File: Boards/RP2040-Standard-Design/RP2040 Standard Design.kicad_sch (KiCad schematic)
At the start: 37 parts, among them J1 BM03B-SRSS-TBLFSN, J3 USB_C, SW1 SW_Push, SW3 SW_Push, U1 ESD7L5.0DT5G, U2 ST1L05APU33R

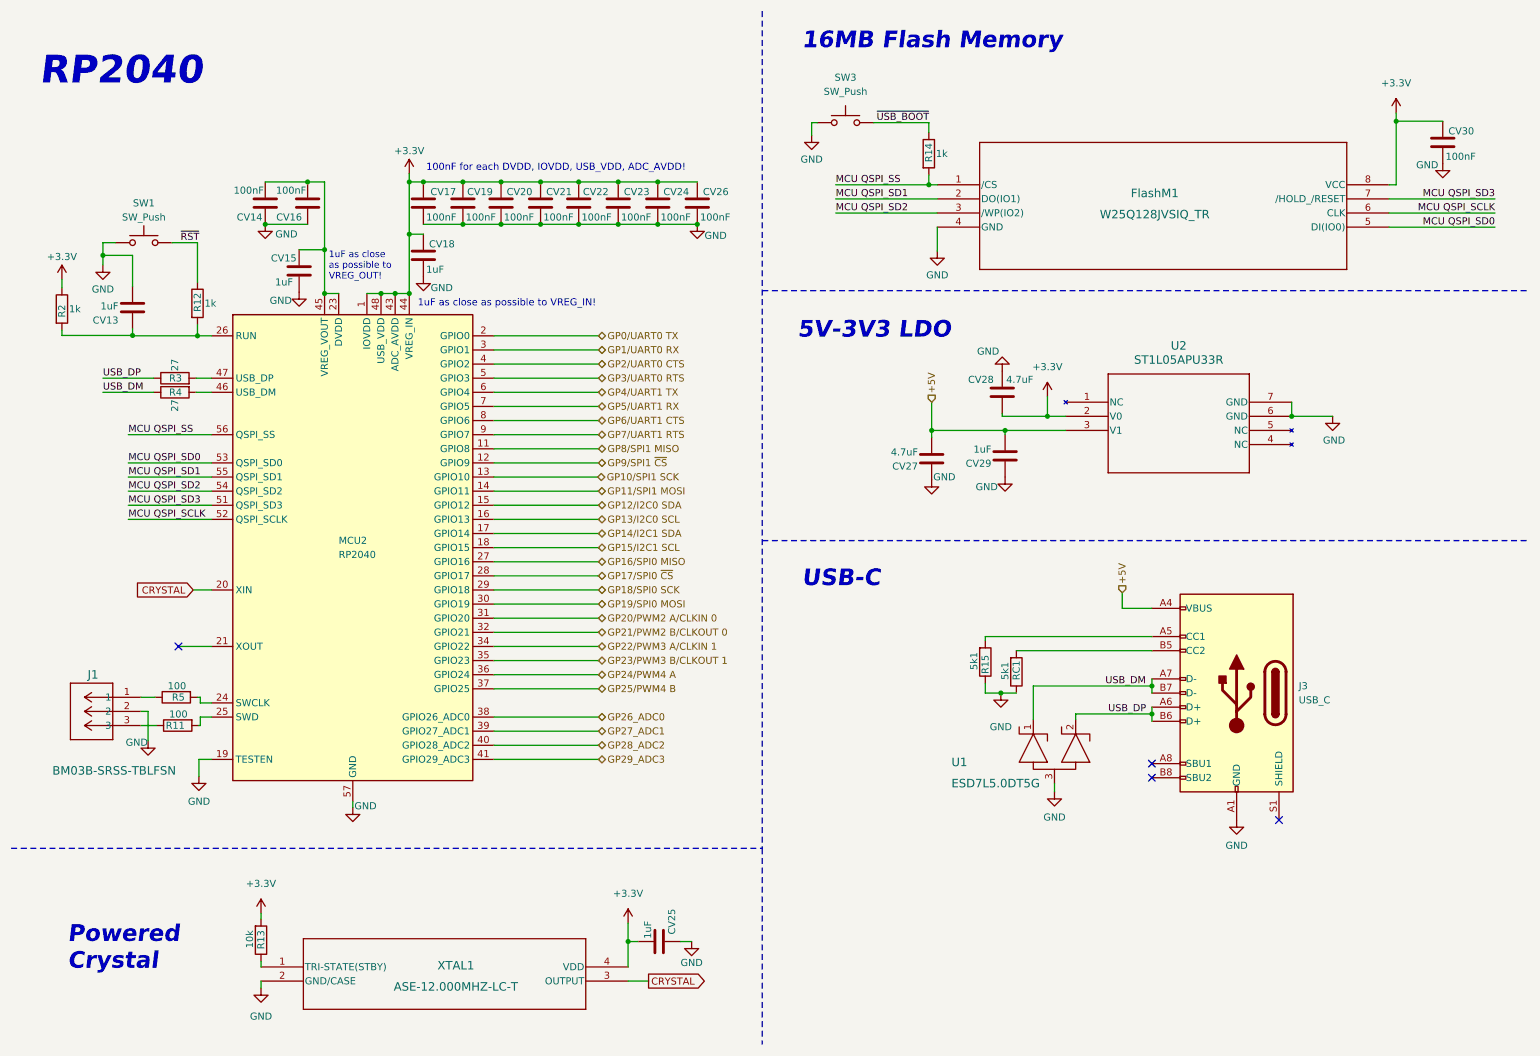
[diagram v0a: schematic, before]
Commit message: Preparação do RP2040 para PCB Design
Foram corrigidos todos os ERC errors e warnings. Foram feitas alterações
aos necessários simbolos, e foi adicionado um botão na biblioteca de
simbolos
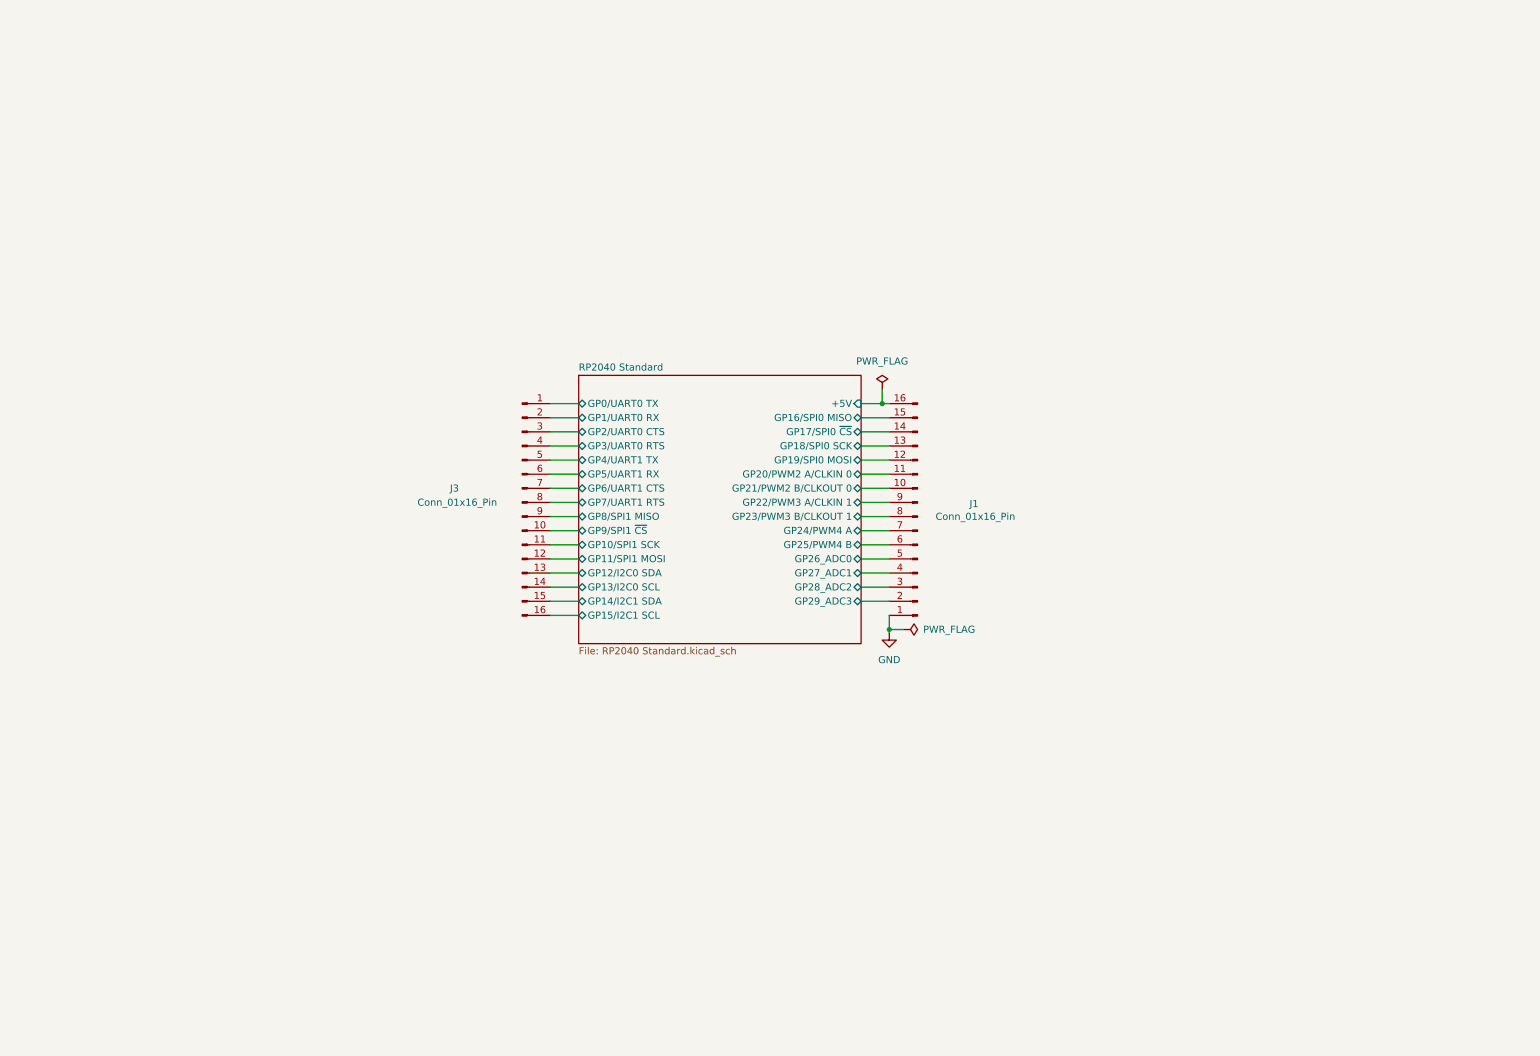
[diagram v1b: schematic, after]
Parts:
- removed CV13, CV15, CV18, CV25, CV29: 1uF, Capacitor_SMD:C_0201_0603Metric, symbol Device:C
- removed CV14, CV16, CV17, CV19, CV20, CV21, CV22, CV23, CV24, CV26, CV30: 100nF, Capacitor_SMD:C_0201_0603Metric, symbol Device:C
- removed CV27, CV28: 4.7uF, Capacitor_SMD:C_0201_0603Metric, symbol Device:C
- removed FlashM1: W25Q128JVSIQ_TR, SOIC_208MIL_WIN, symbol W25Q128JVSIQ TR:W25Q128JVSIQ_TR
- removed J1: BM03B-SRSS-TBLFSN, CONN_BM03B-SRSS-TBLFSN_JST, symbol SWD Con:BM03B-SRSS-TBLFSN
- removed J3: USB_C, Connector_USB:USB_C_Plug_JAE_DX07P024AJ1, symbol Connector:USB_C_Receptacle_USB2.0
- removed MCU2: RP2040, Package_DFN_QFN:QFN-56-1EP_7x7mm_P0.4mm_EP3.2x3.2mm, symbol MCU_RaspberryPi:RP2040
- removed R11, R5: 100, Resistor_SMD:R_0201_0603Metric, symbol Device:R
- removed R12, R14, R2: 1k, Resistor_SMD:R_0201_0603Metric, symbol Device:R
- removed R13: 10k, Resistor_SMD:R_0201_0603Metric, symbol Device:R
- removed R15, RC1: 5k1, Resistor_SMD:R_0201_0603Metric, symbol Device:R
- removed R3, R4: 27, Resistor_SMD:R_0201_0603Metric, symbol Device:R
- removed SW1, SW3: SW_Push, Button_Switch_SMD:SW_Push_1P1T-MP_NO_Horizontal_Alps_SKRTLAE010, symbol Switch:SW_Push
- removed U1: ESD7L5.0DT5G, SOT-723_0P85X1P25_ONS, symbol ESD Protection Diode:ESD7L5.0DT5G
- removed U2: ST1L05APU33R, DFN_5APU33R_STM, symbol LDO 5V.3V3:ST1L05APU33R
- removed XTAL1: ASE-12.000MHZ-LC-T, ASE-3.2X2.5_ABR, symbol AS12MHz:ASE-12.000MHZ-LC-T
- added J1, J3: Conn_01x16_Pin, symbol Connector:Conn_01x16_Pin
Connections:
- net GND: now also J1.1 (Pin_1)
- new net RP2040 Standard/+5V: J1.16 (Pin_16)
- new net RP2040 Standard/GP0/UART0 TX: J3.1 (Pin_1)
- new net RP2040 Standard/GP10/SPI1 SCK: J3.11 (Pin_11)
- new net RP2040 Standard/GP11/SPI1 MOSI: J3.12 (Pin_12)
- new net RP2040 Standard/GP12/I2C0 SDA: J3.13 (Pin_13)
- new net RP2040 Standard/GP13/I2C0 SCL: J3.14 (Pin_14)
- new net RP2040 Standard/GP14/I2C1 SDA: J3.15 (Pin_15)
- new net RP2040 Standard/GP15/I2C1 SCL: J3.16 (Pin_16)
- new net RP2040 Standard/GP16/SPI0 MISO: J1.15 (Pin_15)
- new net RP2040 Standard/GP17/SPI0 ~{CS}: J1.14 (Pin_14)
- new net RP2040 Standard/GP18/SPI0 SCK: J1.13 (Pin_13)
- new net RP2040 Standard/GP19/SPI0 MOSI: J1.12 (Pin_12)
- new net RP2040 Standard/GP1/UART0 RX: J3.2 (Pin_2)
- new net RP2040 Standard/GP20/PWM2 A/CLKIN 0: J1.11 (Pin_11)
- new net RP2040 Standard/GP21/PWM2 B/CLKOUT 0: J1.10 (Pin_10)
- new net RP2040 Standard/GP22/PWM3 A/CLKIN 1: J1.9 (Pin_9)
- new net RP2040 Standard/GP23/PWM3 B/CLKOUT 1: J1.8 (Pin_8)
- new net RP2040 Standard/GP24/PWM4 A: J1.7 (Pin_7)
- new net RP2040 Standard/GP25/PWM4 B: J1.6 (Pin_6)
- new net RP2040 Standard/GP26_ADC0: J1.5 (Pin_5)
- new net RP2040 Standard/GP27_ADC1: J1.4 (Pin_4)
- new net RP2040 Standard/GP28_ADC2: J1.3 (Pin_3)
- new net RP2040 Standard/GP29_ADC3: J1.2 (Pin_2)
- new net RP2040 Standard/GP2/UART0 CTS: J3.3 (Pin_3)
- new net RP2040 Standard/GP3/UART0 RTS: J3.4 (Pin_4)
- new net RP2040 Standard/GP4/UART1 TX: J3.5 (Pin_5)
- new net RP2040 Standard/GP5/UART1 RX: J3.6 (Pin_6)
- new net RP2040 Standard/GP6/UART1 CTS: J3.7 (Pin_7)
- new net RP2040 Standard/GP7/UART1 RTS: J3.8 (Pin_8)
- new net RP2040 Standard/GP8/SPI1 MISO: J3.9 (Pin_9)
- new net RP2040 Standard/GP9/SPI1 ~{CS}: J3.10 (Pin_10)
- no-connect marks 4 -> 0
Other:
- added sheet RP2040 Standard (RP2040 Standard.kicad_sch)
- note removed: "100nF for each DVDD, IOVDD, USB_VDD, ADC_AVDD!"
- note removed: "16MB Flash Memory"
- note removed: "1uF as close as possible to VREG_IN!"
- note removed: "1uF as close as possible to VREG_OUT!"
- note removed: "5V-3V3 LDO"
- note removed: "Powered Crystal"
- note removed: "RP2040"
- note removed: "USB-C"

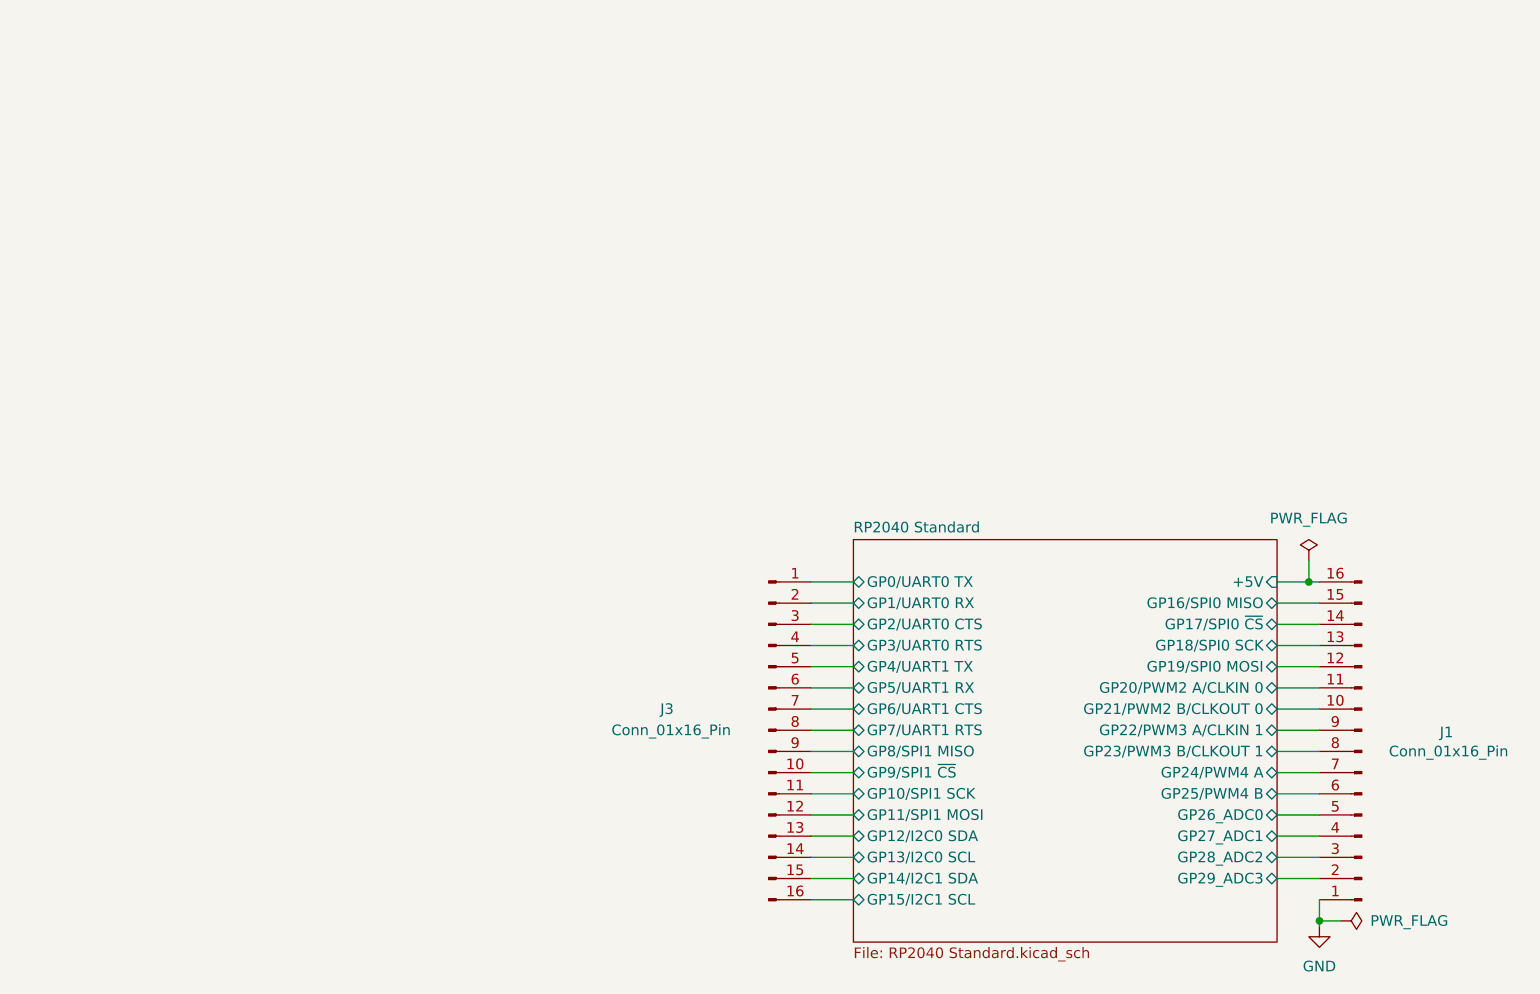
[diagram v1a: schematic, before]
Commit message: USB-C update
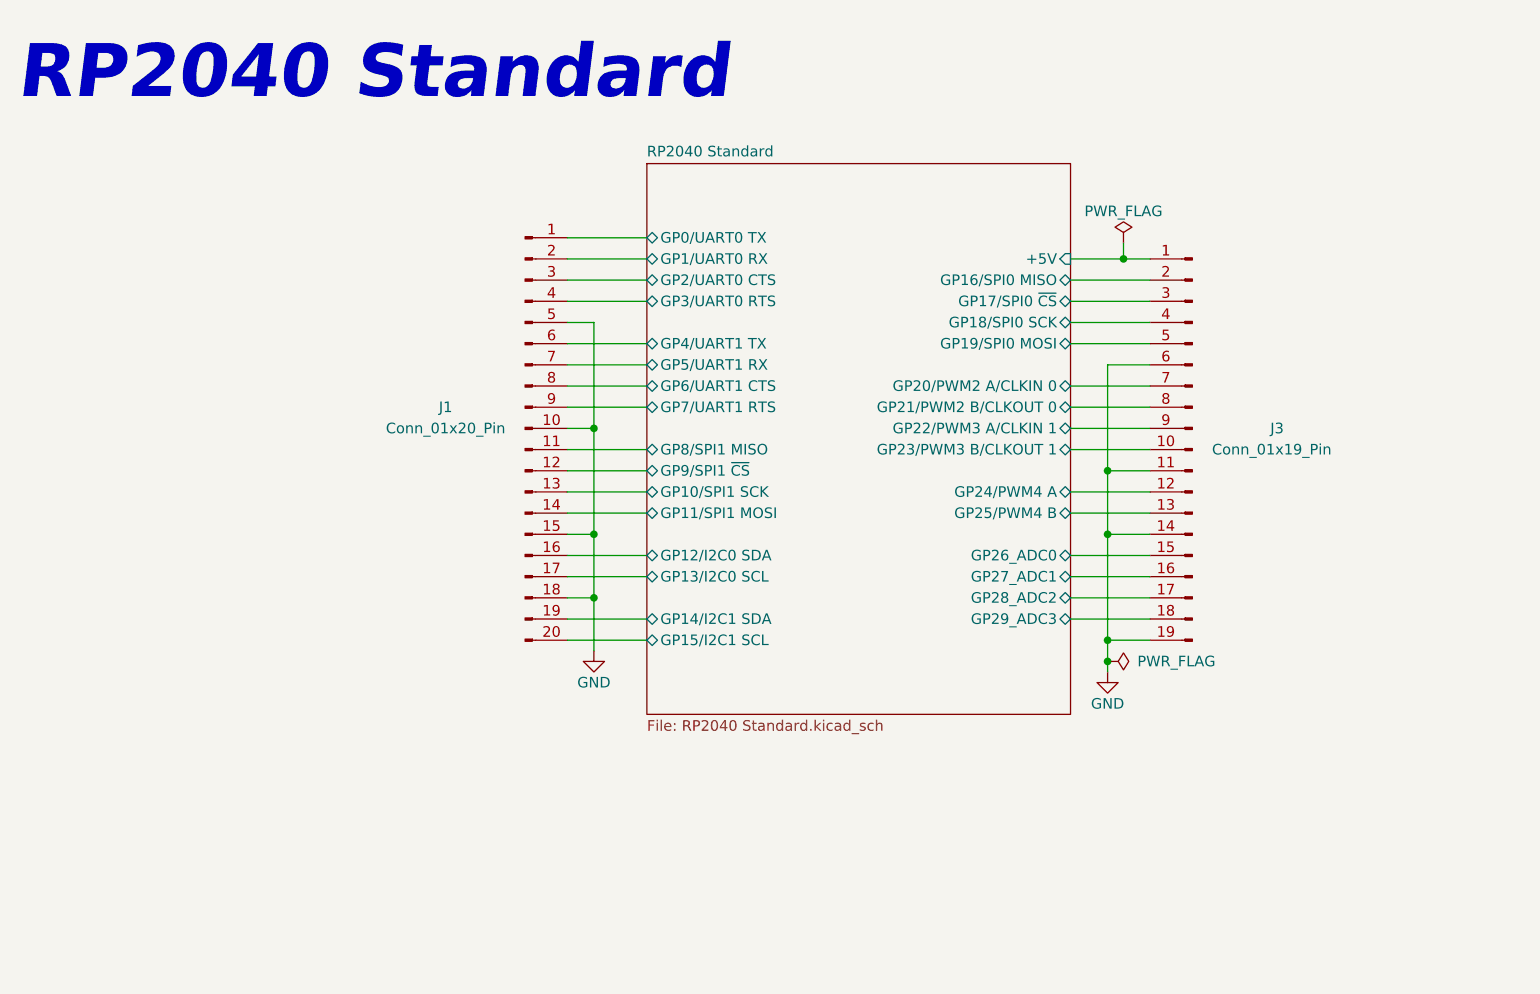
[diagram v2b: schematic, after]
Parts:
- removed J1, J3: Conn_01x16_Pin, symbol Connector:Conn_01x16_Pin
- added J1: Conn_01x20_Pin, symbol Connector:Conn_01x20_Pin
- added J3: Conn_01x19_Pin, symbol Connector:Conn_01x19_Pin
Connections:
- net GND: now also J1.10 (Pin_10), J1.15 (Pin_15), J1.18 (Pin_18), J1.5 (Pin_5), J3.11 (Pin_11), J3.14 (Pin_14), J3.19 (Pin_19), J3.6 (Pin_6)
- net RP2040 Standard/+5V: now also J3.1 (Pin_1)
- net RP2040 Standard/GP0/UART0 TX: now also J1.1 (Pin_1)
- net RP2040 Standard/GP10/SPI1 SCK: now also J1.13 (Pin_13)
- net RP2040 Standard/GP11/SPI1 MOSI: now also J1.14 (Pin_14)
- net RP2040 Standard/GP12/I2C0 SDA: now also J1.16 (Pin_16)
- net RP2040 Standard/GP13/I2C0 SCL: now also J1.17 (Pin_17)
- net RP2040 Standard/GP14/I2C1 SDA: now also J1.19 (Pin_19)
- net RP2040 Standard/GP15/I2C1 SCL: now also J1.20 (Pin_20)
- net RP2040 Standard/GP16/SPI0 MISO: now also J3.2 (Pin_2)
- net RP2040 Standard/GP17/SPI0 ~{CS}: now also J3.3 (Pin_3)
- net RP2040 Standard/GP18/SPI0 SCK: now also J3.4 (Pin_4)
- net RP2040 Standard/GP19/SPI0 MOSI: now also J3.5 (Pin_5)
- net RP2040 Standard/GP1/UART0 RX: now also J1.2 (Pin_2)
- net RP2040 Standard/GP20/PWM2 A/CLKIN 0: now also J3.7 (Pin_7)
- net RP2040 Standard/GP21/PWM2 B/CLKOUT 0: now also J3.8 (Pin_8)
- net RP2040 Standard/GP22/PWM3 A/CLKIN 1: now also J3.9 (Pin_9)
- net RP2040 Standard/GP23/PWM3 B/CLKOUT 1: now also J3.10 (Pin_10)
- net RP2040 Standard/GP24/PWM4 A: now also J3.12 (Pin_12)
- net RP2040 Standard/GP25/PWM4 B: now also J3.13 (Pin_13)
- net RP2040 Standard/GP26_ADC0: now also J3.15 (Pin_15)
- net RP2040 Standard/GP27_ADC1: now also J3.16 (Pin_16)
- net RP2040 Standard/GP28_ADC2: now also J3.17 (Pin_17)
- net RP2040 Standard/GP29_ADC3: now also J3.18 (Pin_18)
- net RP2040 Standard/GP2/UART0 CTS: now also J1.3 (Pin_3)
- net RP2040 Standard/GP3/UART0 RTS: now also J1.4 (Pin_4)
- net RP2040 Standard/GP4/UART1 TX: now also J1.6 (Pin_6)
- net RP2040 Standard/GP5/UART1 RX: now also J1.7 (Pin_7)
- net RP2040 Standard/GP6/UART1 CTS: now also J1.8 (Pin_8)
- net RP2040 Standard/GP7/UART1 RTS: now also J1.9 (Pin_9)
- net RP2040 Standard/GP8/SPI1 MISO: now also J1.11 (Pin_11)
- net RP2040 Standard/GP9/SPI1 ~{CS}: now also J1.12 (Pin_12)
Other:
- note added: "RP2040 Standard"
